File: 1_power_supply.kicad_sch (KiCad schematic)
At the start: 44 parts, among them J101 Conn_01x03_Pin, J102 Conn_01x02_Pin, J103 Conn_01x02_Pin, J104 Conn_01x02_Pin, U101 TPS54332D, U102 TPS561208D, U103 TLV75533PDBV

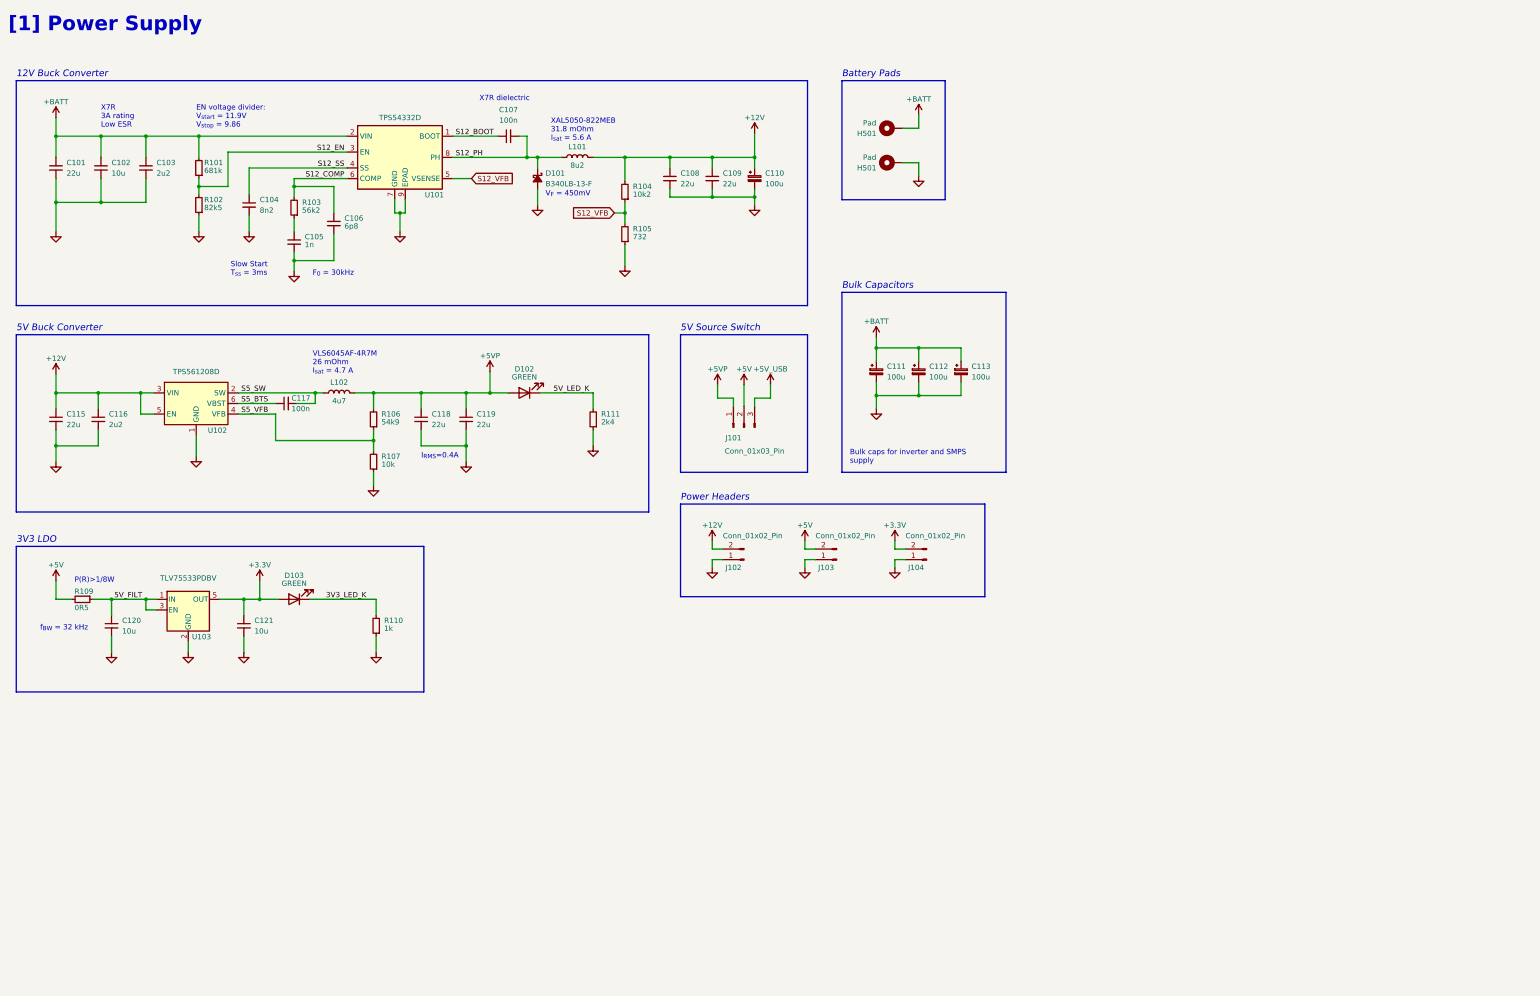
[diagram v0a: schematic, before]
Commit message: feat: major circuit rework, style update and addition of a few extra subcomponents
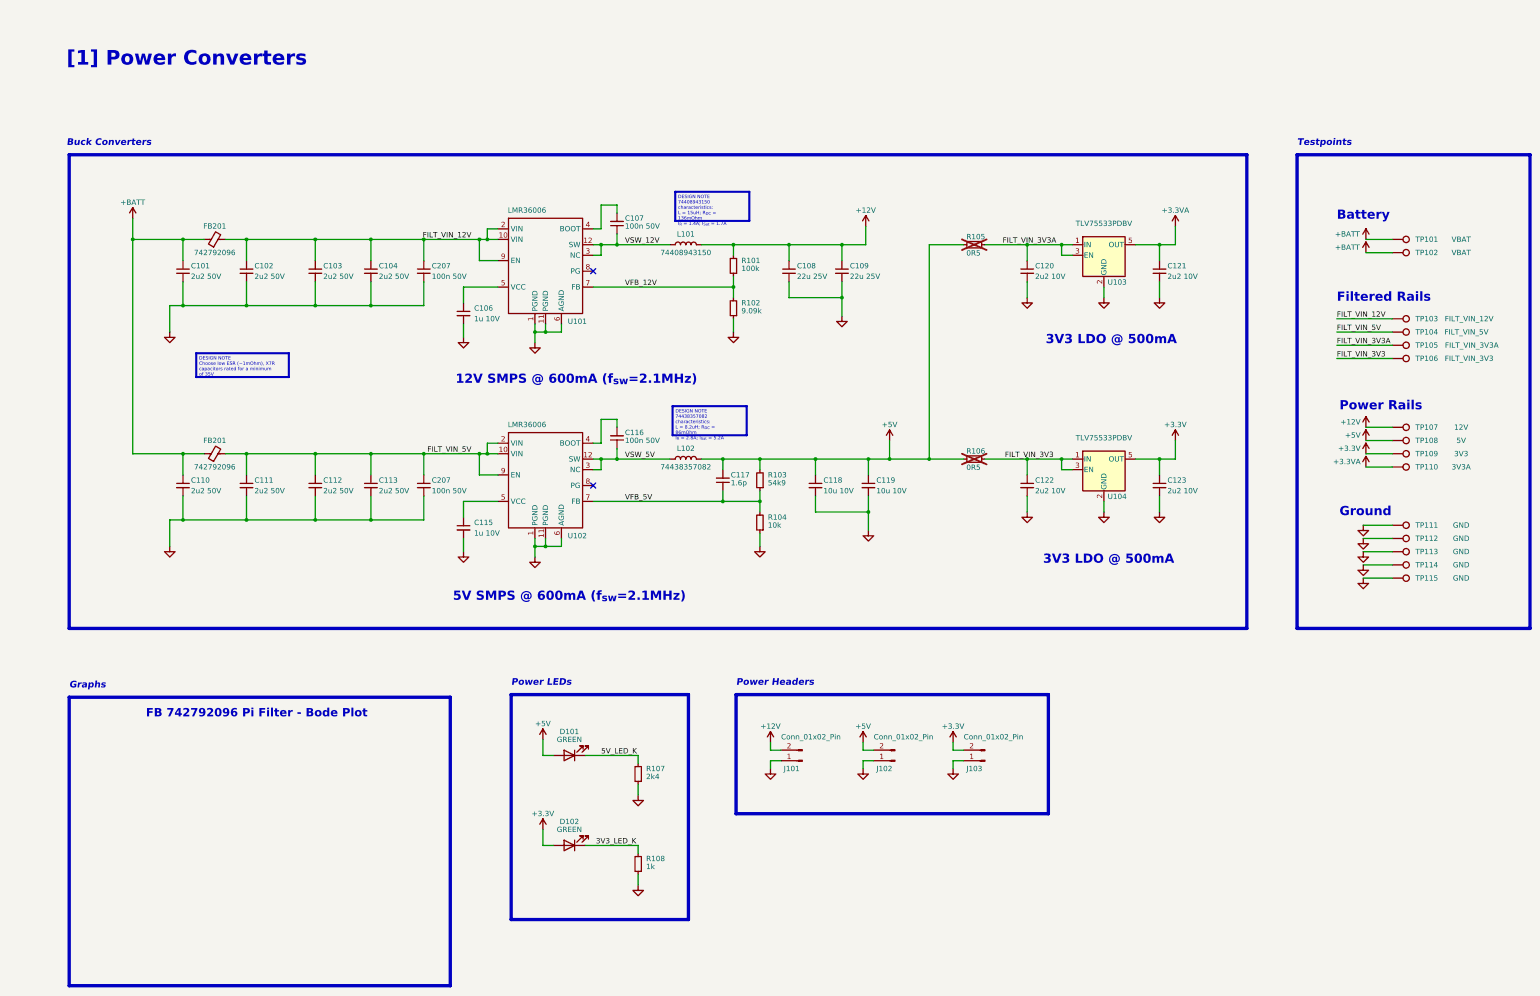
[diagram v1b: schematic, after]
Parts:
- removed C105: 1n, Capacitor_SMD:C_0402_1005Metric_Pad0.74x0.62mm_HandSolder, symbol Device:C_Small
- removed C110, C111, C112, C113: 100u, Capacitor_SMD:CP_Elec_6.3x7.7, symbol Device:C_Polarized_Small
- removed D101: B340LB-13-F, Diode_SMD:D_SOD-123, symbol Device:D_Schottky_Small_Filled
- removed D103: GREEN, LED_SMD:LED_0603_1608Metric_Pad1.05x0.95mm_HandSolder, symbol Device:LED
- removed H501 (x2): Pad, TestPoint:TestPoint_THTPad_4.0x4.0mm_Drill2.0mm, symbol Mechanical:MountingHole_Pad
- removed J101: Conn_01x03_Pin, Connector_PinHeader_2.54mm:PinHeader_1x03_P2.54mm_Vertical, symbol Connector:Conn_01x03_Pin
- removed J104: Conn_01x02_Pin, Connector_PinHeader_2.54mm:PinHeader_1x02_P2.54mm_Vertical, symbol Connector:Conn_01x02_Pin
- removed R109: 0R5, Resistor_SMD:R_0603_1608Metric_Pad0.98x0.95mm_HandSolder, symbol Device:R_Small
- removed R110: 1k, Resistor_SMD:R_0603_1608Metric_Pad0.98x0.95mm_HandSolder, symbol Device:R_Small
- removed R111: 2k4, Resistor_SMD:R_0603_1608Metric_Pad0.98x0.95mm_HandSolder, symbol Device:R_Small
- removed U101: TPS54332D, Package_SO:TI_SO-PowerPAD-8, symbol Regulator_Switching:TPS54332D
- removed U102: TPS561208D, Package_TO_SOT_SMD:SOT-23-6, symbol Regulator_Switching:TPS561208D
- added C110, C111, C112, C113: 2u2 50V, Capacitor_SMD:C_0603_1608Metric_Pad1.08x0.95mm_HandSolder, symbol Device:C_Small
- added C122, C123: 2u2 10V, Capacitor_SMD:C_0603_1608Metric_Pad1.08x0.95mm_HandSolder, symbol Device:C_Small
- added C207 (x2): 100n 50V, Capacitor_SMD:C_0402_1005Metric_Pad0.74x0.62mm_HandSolder, symbol Device:C_Small
- added D101: GREEN, LED_SMD:LED_0603_1608Metric_Pad1.05x0.95mm_HandSolder, symbol Device:LED
- added FB201 (x2): 742792096, Inductor_SMD:L_0805_2012Metric_Pad1.05x1.20mm_HandSolder, symbol Device:FerriteBead_Small
- added J101: Conn_01x02_Pin, Connector_PinHeader_2.54mm:PinHeader_1x02_P2.54mm_Vertical, symbol Connector:Conn_01x02_Pin
- added R108: 1k, Resistor_SMD:R_0603_1608Metric_Pad0.98x0.95mm_HandSolder, symbol Device:R_Small
- added TP101, TP102: VBAT, TestPoint:TestPoint_Pad_D1.5mm, symbol Connector:TestPoint
- added TP103: FILT_VIN_12V, TestPoint:TestPoint_Pad_D1.5mm, symbol Connector:TestPoint
- added TP104: FILT_VIN_5V, TestPoint:TestPoint_Pad_D1.5mm, symbol Connector:TestPoint
- added TP105: FILT_VIN_3V3A, TestPoint:TestPoint_Pad_D1.5mm, symbol Connector:TestPoint
- added TP106: FILT_VIN_3V3, TestPoint:TestPoint_Pad_D1.5mm, symbol Connector:TestPoint
- added TP107: 12V, TestPoint:TestPoint_Pad_D1.5mm, symbol Connector:TestPoint
- added TP108: 5V, TestPoint:TestPoint_Pad_D1.5mm, symbol Connector:TestPoint
- added TP109: 3V3, TestPoint:TestPoint_Pad_D1.5mm, symbol Connector:TestPoint
- added TP110: 3V3A, TestPoint:TestPoint_Pad_D1.5mm, symbol Connector:TestPoint
- added TP111, TP112, TP113, TP114, TP115: GND, TestPoint:TestPoint_Pad_D1.5mm, symbol Connector:TestPoint
- added U101, U102: LMR36006, LMR36006:RNX0012B, symbol Regulator_Switching:LMR36006
- added U104: TLV75533PDBV, Package_TO_SOT_SMD:SOT-23-5, symbol Regulator_Linear:TLV75533PDBV
- C101: value 22u -> 2u2 50V; Link (none) -> https://www.digikey.de/en/products/detail/tdk-corporation/C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
- C102: value 10u -> 2u2 50V; Link (none) -> https://www.digikey.de/en/products/detail/tdk-corporation/C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
- C103: value 2u2 -> 2u2 50V; Link (none) -> https://www.digikey.de/en/products/detail/tdk-corporation/C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
- C104: value 8n2 -> 2u2 50V; footprint Capacitor_SMD:C_0402_1005Metric_Pad0.74x0.62mm_HandSolder -> Capacitor_SMD:C_0603_1608Metric_Pad1.08x0.95mm_HandSolder; Link (none) -> https://www.digikey.de/en/products/detail/tdk-corporation/C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
- C106: value 6p8 -> 1u 10V; footprint Capacitor_SMD:C_0402_1005Metric_Pad0.74x0.62mm_HandSolder -> Capacitor_SMD:C_0603_1608Metric_Pad1.08x0.95mm_HandSolder
- C107: value 100n -> 100n 50V
- C108, C109: value 22u -> 22u 25V; Link (none) -> https://www.digikey.de/en/products/detail/murata-electronic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
- C115: value 22u -> 1u 10V
- C116: value 2u2 -> 100n 50V; footprint Capacitor_SMD:C_0603_1608Metric_Pad1.08x0.95mm_HandSolder -> Capacitor_SMD:C_0402_1005Metric_Pad0.74x0.62mm_HandSolder
- C117: value 100n -> 1.6p
- C118, C119: value 22u -> 10u 10V; Link (none) -> https://www.digikey.de/en/products/detail/tdk-corporation/C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
- C120, C121: value 10u -> 2u2 10V; Link (none) -> https://www.digikey.de/en/products/detail/murata-electronic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
- L101: value 8u2 -> 74408943150; footprint Inductor_SMD:L_Coilcraft_XAL5050-XXX -> Inductor_SMD_Wurth:74408943150; Link https://www.mouser.de/ProductDetail/Coilcraft/XAL5050-822ME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 -> https://www.digikey.de/en/products/detail/w%C3%BCrth-elektr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
- L102: value 4u7 -> 74438357082; footprint Inductor_SMD:L_TDK_VLS6045EX_VLS6045AF -> Inductor_SMD_Wurth:74438357082; Link https://www.digikey.de/en/products/detail/tdk-corporation/V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 -> https://www.digikey.de/en/products/detail/w%C3%BCrth-elektr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
- R101: value 681k -> 100k
- R102: value 82k5 -> 9.09k
- R103: value 56k2 -> 54k9; footprint Resistor_SMD:R_0402_1005Metric_Pad0.72x0.64mm_HandSolder -> Resistor_SMD:R_0603_1608Metric_Pad0.98x0.95mm_HandSolder
- R104: value 10k2 -> 10k
- R105: value 732 -> 0R5; now not fitted
- R106: value 54k9 -> 0R5; now not fitted
- R107: value 10k -> 2k4
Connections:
- net S5_BTS is gone; now on net VFB_5V: C117.1
- net +12V: now also R101.2, J101.2 (Pin_2), TP107.1; no longer C115.1, C116.1, J102.2 (Pin_2), R104.2
- net +3.3V: now also D102.2 (A), J103.2 (Pin_2), C123.1, TP109.1, U104.5 (OUT); no longer C121.1, U103.5 (OUT)
- net +5V: now also C117.2, C118.1, C119.1, J102.2 (Pin_2), L102.2, R103.2, R105.2, R106.2, D101.2 (A), TP108.1; no longer J103.2 (Pin_2)
- net +BATT: now also C110.1, FB201.1, FB201.1, TP101.1, TP102.1; no longer C102.1, C103.1, R101.2
- net 3V3_LED_K: now also D102.1 (K), R108.2
- net 5V_LED_K: now also R107.2, D101.1 (K); no longer D102.1 (K)
- net GND: now also R104.1, C110.2, C111.2, C112.2, C113.2, C122.2, C123.2, C207.2, C207.2, J101.1 (Pin_1), R108.1, TP111.1, TP112.1, TP113.1, TP114.1, TP115.1, U101.1 (PGND), U101.11 (PGND), U101.6 (AGND), U102.1 (PGND), U102.11 (PGND), U102.6 (AGND), U104.2 (GND); no longer C116.2, R105.1
- net VFB_5V: now reaches R103.1
- net VFB_5V: now also R104.2, U102.7 (FB)
- removed net +5VP: C118.1, C119.1, D102.2 (A), L102.2, R106.2
- net 5V_FILT renamed FILT_VIN_3V3A
- net FILT_VIN_3V3A: now also R105.1, TP105.1
- net S12_BOOT renamed VSW_12V
- net VSW_12V: now also L101.1, U101.12 (SW), U101.3 (NC)
- net S12_COMP: no longer names the net of C106.1
- net S12_COMP: now also U101.5 (VCC); no longer R103.2
- net S12_EN renamed VFB_12V
- net VFB_12V: now also U101.7 (FB)
- net S12_PH: no longer names the net of C107.2
- net S12_PH: now also U101.4 (BOOT); no longer L101.1
- net S12_SS renamed FILT_VIN_12V
- net FILT_VIN_12V: now also C102.1, C103.1, C207.1, FB201.2, TP103.1, U101.10 (VIN), U101.2 (VIN), U101.9 (EN)
- removed net S12_VFB: R104.1, R105.2
- net S5_SW renamed VSW_5V
- net VSW_5V: now also C116.1, U102.12 (SW), U102.3 (NC); no longer C117.2
- net S5_VFB renamed FILT_VIN_3V3
- net FILT_VIN_3V3: now also C122.1, TP106.1, U104.1 (IN), U104.3 (EN); no longer R107.2
- new net: C116.2, U102.4 (BOOT)
- new net: C115.1, U102.5 (VCC)
- new net +3.3VA: C121.1, TP110.1, U103.5 (OUT)
- new net FILT_VIN_5V: C111.1, C112.1, C113.1, C207.1, FB201.2, TP104.1, U102.10 (VIN), U102.2 (VIN), U102.9 (EN)
- no-connect marks 0 -> 2
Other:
- note added: "12V SMPS @ 600mA (f_{sw}=2.1MHz)"
- note added: "3V3 LDO @ 500mA"
- note added: "5V SMPS @ 600mA (f_{sw}=2.1MHz)"
- note added: "Battery"
- note added: "Buck Converters"
- note added: "FB 742792096 Pi Filter - Bode Plot"
- note added: "Filtered Rails"
- note added: "Graphs"
- note added: "Ground"
- note added: "Power LEDs"
- note added: "Power Rails"
- note added: "Testpoints"
- note added: "[1] Power Converters"
- note removed: "12V Buck Converter"
- note removed: "3V3 LDO"
- note removed: "5V Buck Converter"
- note removed: "5V Source Switch"
- note removed: "Battery Pads"
- note removed: "Bulk Capacitors"
- note removed: "Bulk caps for inverter and SMPS supply"
- note removed: "EN voltage divider: V_{start} = 11.9V V_{stop} = 9.86"
- note removed: "F_{0} = 30kHz"
- note removed: "I_{RMS}=0.4A"
- note removed: "P(R)>1/8W"
- note removed: "Slow Start T_{ss} = 3ms"
- note removed: "VLS6045AF-4R7M 26 mOhm I_{sat} = 4.7 A"
- note removed: "V_{F} = 450mV"
- note removed: "X7R 3A rating Low ESR"
- note removed: "X7R dielectric"
- note removed: "XAL5050-822MEB 31.8 mOhm I_{sat} = 5.6 A"
- note removed: "[1] Power Supply"
- note removed: "f_{BW} = 32 kHz"
- title: Power Supply -> Power Converters

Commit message: feat: component placement, again
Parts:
- C101, C102, C103, C104, C110, C111, C112, C113: footprint Capacitor_SMD:C_0603_1608Metric_Pad1.08x0.95mm_HandSolder -> Capacitor_SMD:C_0805_2012Metric_Pad1.18x1.45mm_HandSolder
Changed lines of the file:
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@@
     (data
       iVBORw0KGgoAAAANSUhEUgAADbUAAAmwCAIAAACY8LCZAAAAA3NCSVQICAjb4U/gAAAACXBIWXMA
-      AAsSAAALEgHS3X78AAAgAElEQVR4nOzdW4sbSRaF0R2R5TbM//+zHpci+iFTKrnnAmN3YbRnLQpb
+      AArwAAAK8AFCrDSYAAAgAElEQVR4nOzdW4sbSRaF0R2R5TbM//+zHpci+iFTKrnnAmN3YbRnLQpb
       dwSpp+TLc8beOwAAAAAAAAAAAABF5u/+AgAAAAAAAAAAAAB/M30kAAAAAAAAAAAA0EYfCQAAAAAA
       AAAAALTRRwIAAAAAAAAAAABt9JEAAAAAAAAAAABAG30kAAAAAAAAAAAA0EYfCQAAAAAAAAAAALTR
@@
       (effects (font (size 1.27 1.27)) (justify left))
     )
-    (property "Footprint" "Capacitor_SMD:C_0603_1608Metric_Pad1.08x0.95mm_HandSolder" (at 105.41 82.55 0)
+    (property "Footprint" "Capacitor_SMD:C_0805_2012Metric_Pad1.18x1.45mm_HandSolder" (at 105.41 82.55 0)
       (effects (font (size 1.27 1.27)) hide)
     )
@@
       (effects (font (size 1.27 1.27)) (justify left))
     )
-    (property "Footprint" "Capacitor_SMD:C_0603_1608Metric_Pad1.08x0.95mm_HandSolder" (at 92.075 133.985 0)
+    (property "Footprint" "Capacitor_SMD:C_0805_2012Metric_Pad1.18x1.45mm_HandSolder" (at 92.075 133.985 0)
       (effects (font (size 1.27 1.27)) hide)
     )
@@
       (effects (font (size 1.27 1.27)) (justify left))
     )
-    (property "Footprint" "Capacitor_SMD:C_0603_1608Metric_Pad1.08x0.95mm_HandSolder" (at 75.565 133.985 0)
+    (property "Footprint" "Capacitor_SMD:C_0805_2012Metric_Pad1.18x1.45mm_HandSolder" (at 75.565 133.985 0)
       (effects (font (size 1.27 1.27)) hide)
     )
@@
       (effects (font (size 1.27 1.27)) (justify left))
     )
-    (property "Footprint" "Capacitor_SMD:C_0603_1608Metric_Pad1.08x0.95mm_HandSolder" (at 60.325 82.55 0)
+    (property "Footprint" "Capacitor_SMD:C_0805_2012Metric_Pad1.18x1.45mm_HandSolder" (at 60.325 82.55 0)
       (effects (font (size 1.27 1.27)) hide)
     )
@@
       (effects (font (size 1.27 1.27)) (justify left))
     )
-    (property "Footprint" "Capacitor_SMD:C_0603_1608Metric_Pad1.08x0.95mm_HandSolder" (at 75.565 82.55 0)
+    (property "Footprint" "Capacitor_SMD:C_0805_2012Metric_Pad1.18x1.45mm_HandSolder" (at 75.565 82.55 0)
       (effects (font (size 1.27 1.27)) hide)
     )
@@
       (effects (font (size 1.27 1.27)) (justify left))
     )
-    (property "Footprint" "Capacitor_SMD:C_0603_1608Metric_Pad1.08x0.95mm_HandSolder" (at 92.075 82.55 0)
+    (property "Footprint" "Capacitor_SMD:C_0805_2012Metric_Pad1.18x1.45mm_HandSolder" (at 92.075 82.55 0)
       (effects (font (size 1.27 1.27)) hide)
     )
@@
       (effects (font (size 1.27 1.27)) (justify left))
     )
-    (property "Footprint" "Capacitor_SMD:C_0603_1608Metric_Pad1.08x0.95mm_HandSolder" (at 105.41 133.985 0)
+    (property "Footprint" "Capacitor_SMD:C_0805_2012Metric_Pad1.18x1.45mm_HandSolder" (at 105.41 133.985 0)
       (effects (font (size 1.27 1.27)) hide)
     )
@@
       (effects (font (size 1.27 1.27)) (justify left))
     )
-    (property "Footprint" "Capacitor_SMD:C_0603_1608Metric_Pad1.08x0.95mm_HandSolder" (at 60.325 133.985 0)
+    (property "Footprint" "Capacitor_SMD:C_0805_2012Metric_Pad1.18x1.45mm_HandSolder" (at 60.325 133.985 0)
       (effects (font (size 1.27 1.27)) hide)
     )

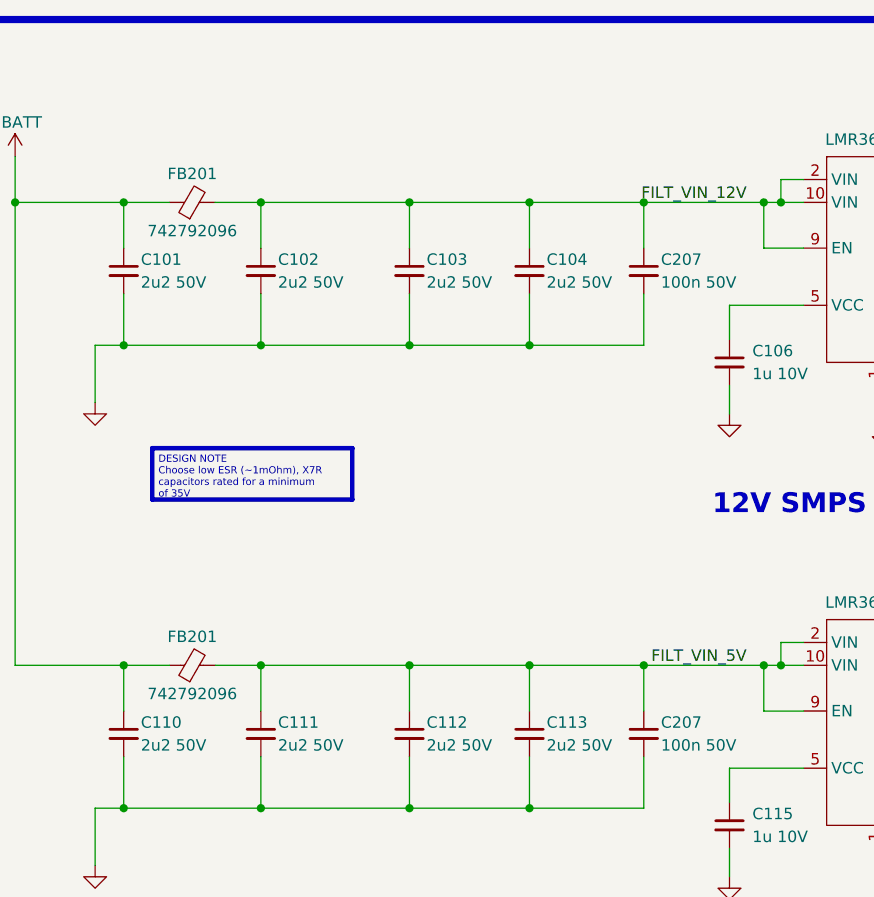
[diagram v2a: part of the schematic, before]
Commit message: feat: finished inverter placement and routing
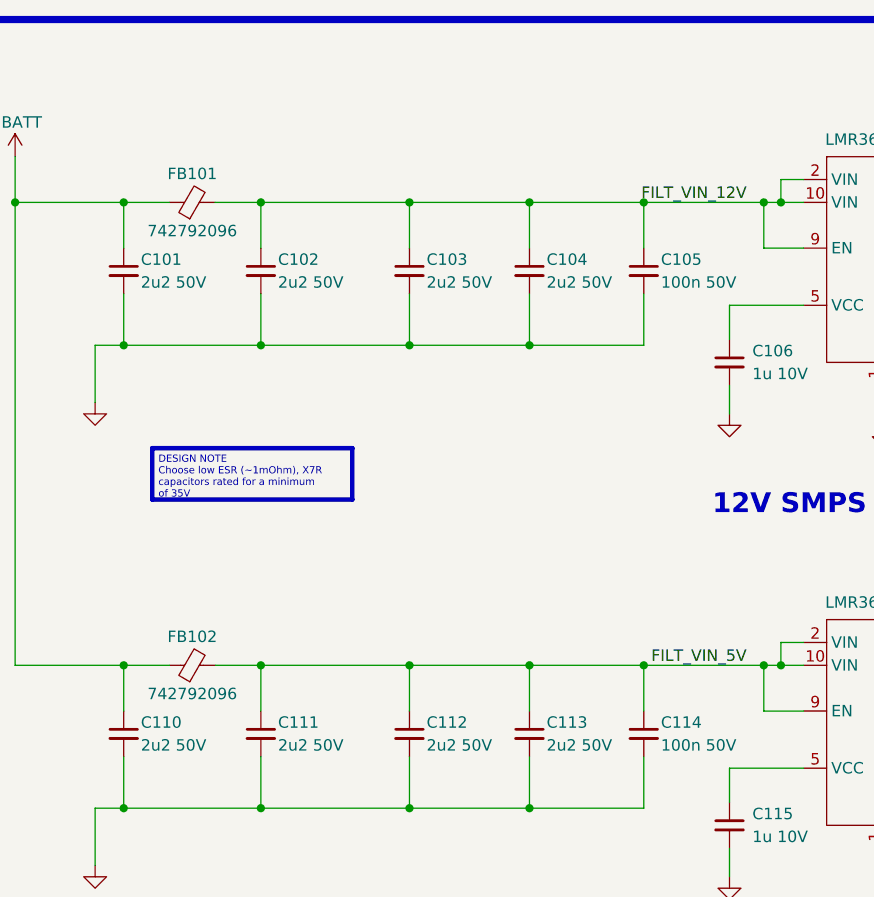
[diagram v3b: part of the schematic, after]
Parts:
- TP101, TP102, TP103, TP104, TP105, TP106, TP107, TP108, TP109, TP110, TP111, TP112, TP113, TP114, TP115: footprint TestPoint:TestPoint_Pad_D1.5mm -> TestPoint:TestPoint_Pad_D1.0mm
- renumbered C207 to C105, C207 to C114, FB201 to FB101, FB201 to FB102
